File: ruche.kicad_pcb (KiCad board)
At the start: 2 copper layers, 61 x 100 mm, 68 parts, among them IC1 CN3791, IC2 MAX17048G+, IC3 L86-M33, IC4 SHT41-AD1B-R3, J1 Conn_01x02, J10 Conn_01x04, J11 Conn_01x04, J12 Conn_01x04, J13 Micro_SD_Card, J2 Conn_01x04, J3 Conn_01x03, J4 Conn_01x04, J5 Conn_01x04, J6 Conn_01x02, J7 Conn_01x02, J8 Conn_01x03, J9 Conn_01x03, Q1 AO3401A, U1 MKRWAN_1310, U2 MS5611-01BA, U3 XC6220B331MR

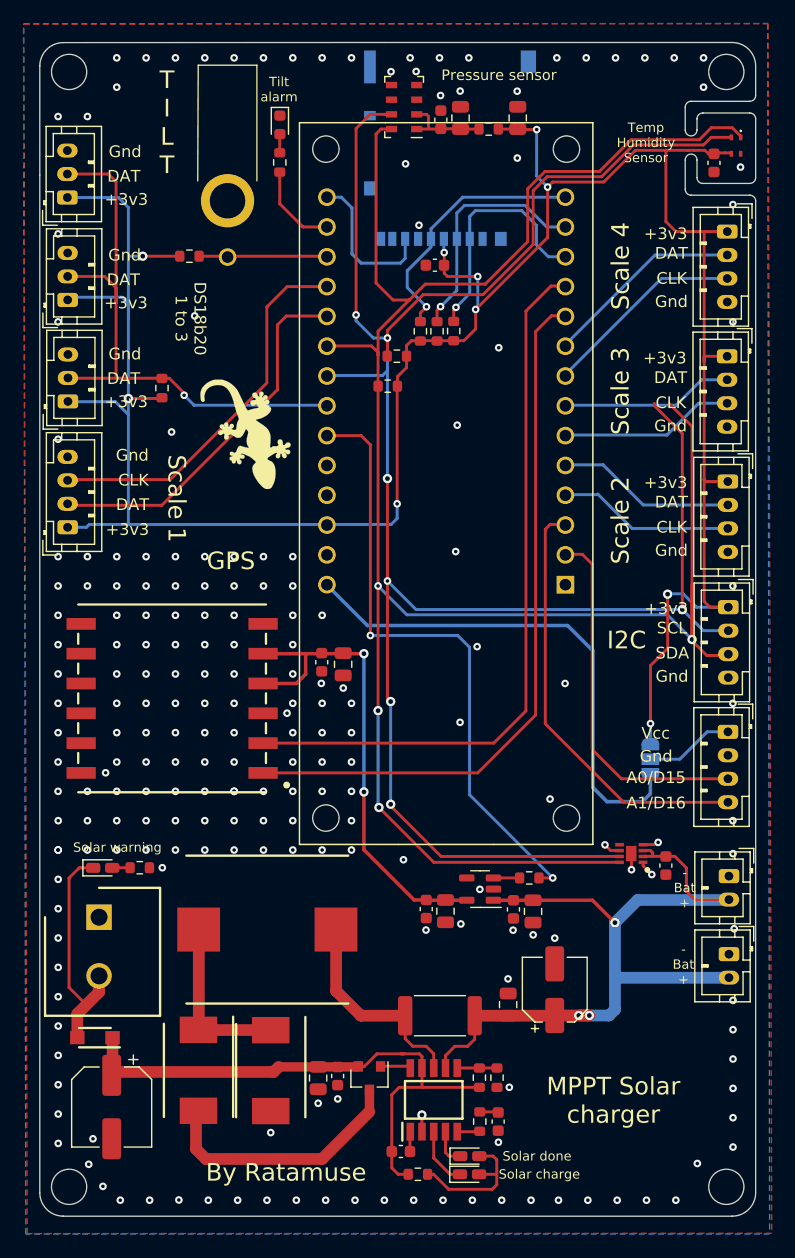
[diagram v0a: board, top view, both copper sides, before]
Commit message: Changement des pins
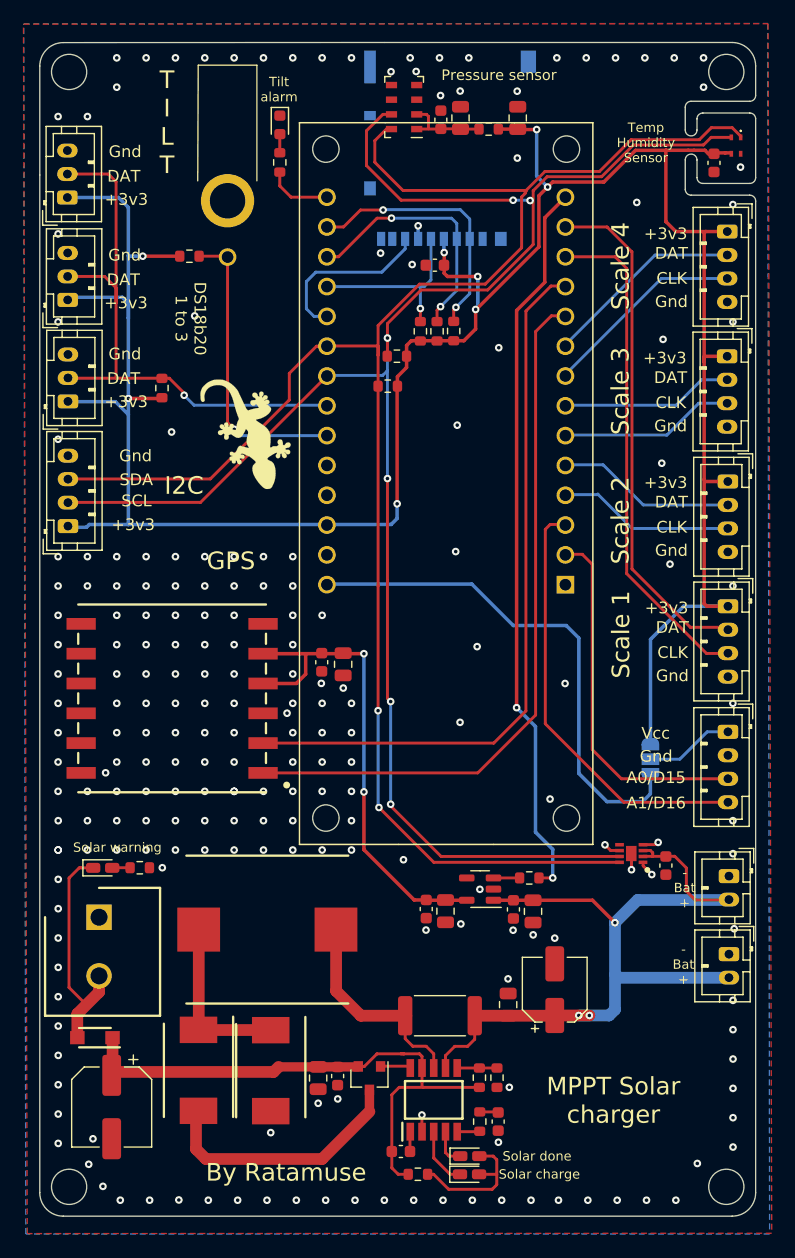
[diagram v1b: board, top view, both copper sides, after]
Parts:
- moved J5 56.7 mm to (98.9, 110.3), turned to 90 degrees
- moved J2 56.7 mm to (155.1, 117.1), turned to -90 degrees
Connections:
- U1 pad 12: SD3-CS-D6 -> CLK1
- U1 pad 13: CMD-MOSI-D3 -> DAT1
- U1 pad 14: CLK-SCK-D4 -> Start_GPS
- U1 pad 15: SDO-MISO-D5 -> Tilt_led_alarm
- U1 pad 16: Tilt_led_alarm -> SD3-CS-D6
- U1 pad 17: INT1 -> CMD-MOSI-D3
- U1 pad 18: CLK1 -> CLK-SCK-D4
- U1 pad 19: DAT1 -> SDO-MISO-D5
- U1 pad 23: Start_GPS -> INT1
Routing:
- net SDA: track 185.1 -> 155.3 mm, vias 4 -> 2
- net SCL: track 180.8 -> 155.3 mm, vias 7 -> 6
- net INT1: track 11.0 -> 25.7 mm, vias 0 -> 1
- net DAT1: track 32.2 -> 43.9 mm
- net CLK1: track 33.1 -> 43.1 mm
- net Start_GPS: track 52.9 -> 62.2 mm
- net CLK-SCK-D4: track 22.5 -> 15.5 mm
- net +3V3: track 219.9 -> 217.6 mm, vias 10 -> 8
- net Tilt_led_alarm: track 7.54 -> 5.59 mm
- net SD3-CS-D6: track 20.5 -> 22.4 mm, vias 1 -> 2
- net SDO-MISO-D5: track 13.1 -> 14.8 mm
- net CMD-MOSI-D3: track 20.2 -> 21.7 mm, vias 1 -> 2
- net GND: track 7.00 -> 8.10 mm, vias 214 -> 219

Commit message: Modification routage
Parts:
- moved C18 1.73 mm to (129.3, 143.1)
- moved C17 1.72 mm to (131.2, 143.0)
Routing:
- net GND: track 8.10 -> 9.33 mm, vias 219 -> 218

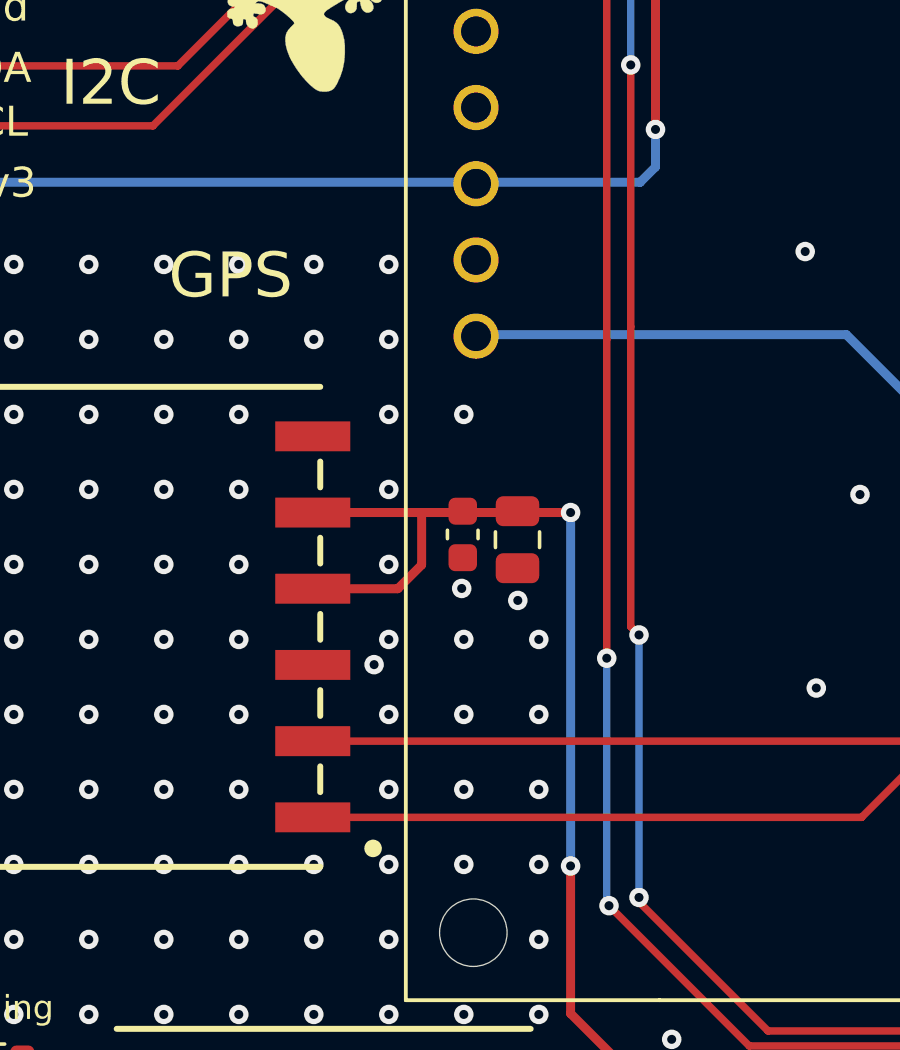
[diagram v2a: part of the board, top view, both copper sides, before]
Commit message: Add GPS backup power supply
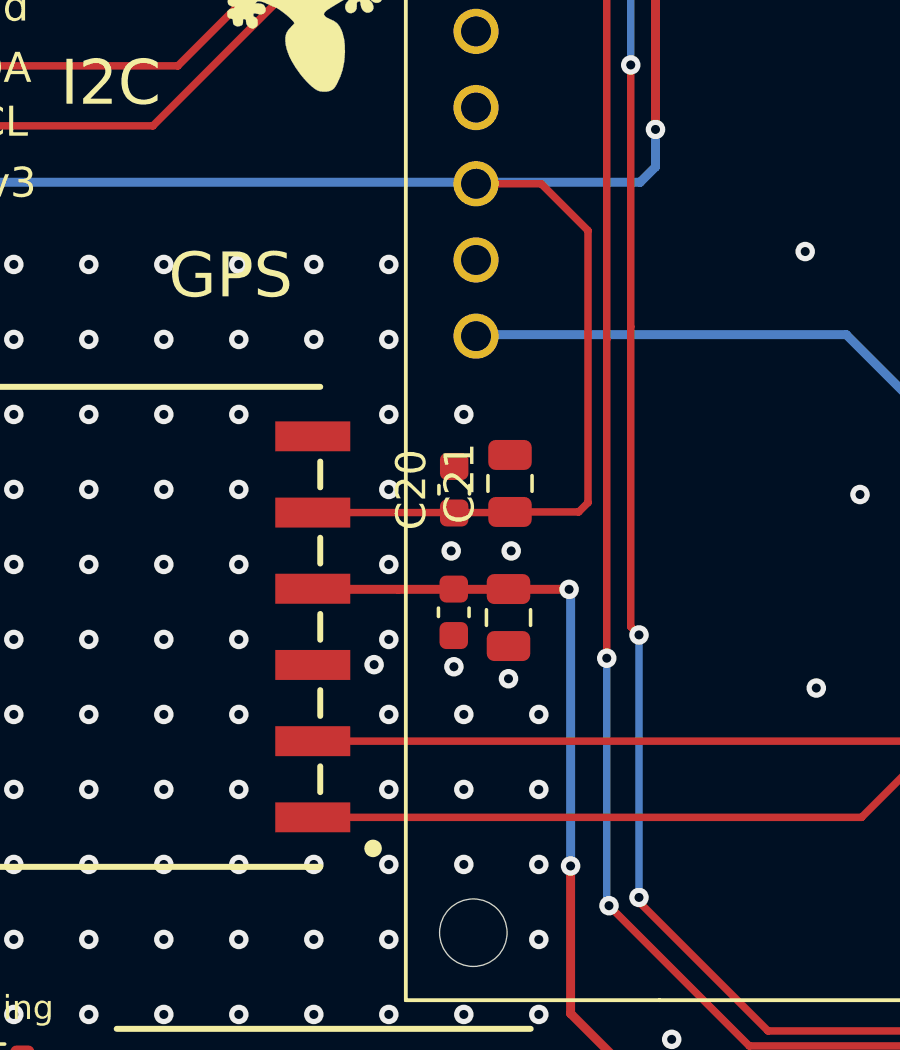
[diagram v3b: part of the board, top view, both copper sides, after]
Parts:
- added C20: 0.1µF, Capacitor_SMD:C_0603_1608Metric, F.Cu at (120.2, 120.4)
- added C21: 10µF, Capacitor_SMD:C_0805_2012Metric, F.Cu at (122.1, 120.2)
- moved C11 2.61 mm to (122.0, 124.7)
- moved C6 2.61 mm to (120.2, 124.5)
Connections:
- net CLK-SCK-D4 renamed CLK-SCK-D9
- net CMD-MOSI-D3 renamed CMD-MOSI-D8
- net SD3-CS-D6 renamed SD3-CS-D7
- net SDO-MISO-D5 renamed SDO-MISO-D10
- IC3 pad 5: VCC_GPS -> +3V3
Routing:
- net +3V3: track 217.6 -> 240.3 mm
- net VCC_GPS: track 45.2 -> 33.2 mm

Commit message: Add graphics
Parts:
- added G***: LOGO, Empreintes:bee, F.Cu at (150.0, 158.7)
- added G***: LOGO, Empreintes:bee large, B.Cu at (110.4, 100.3)
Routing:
- net GND: vias 218 -> 215

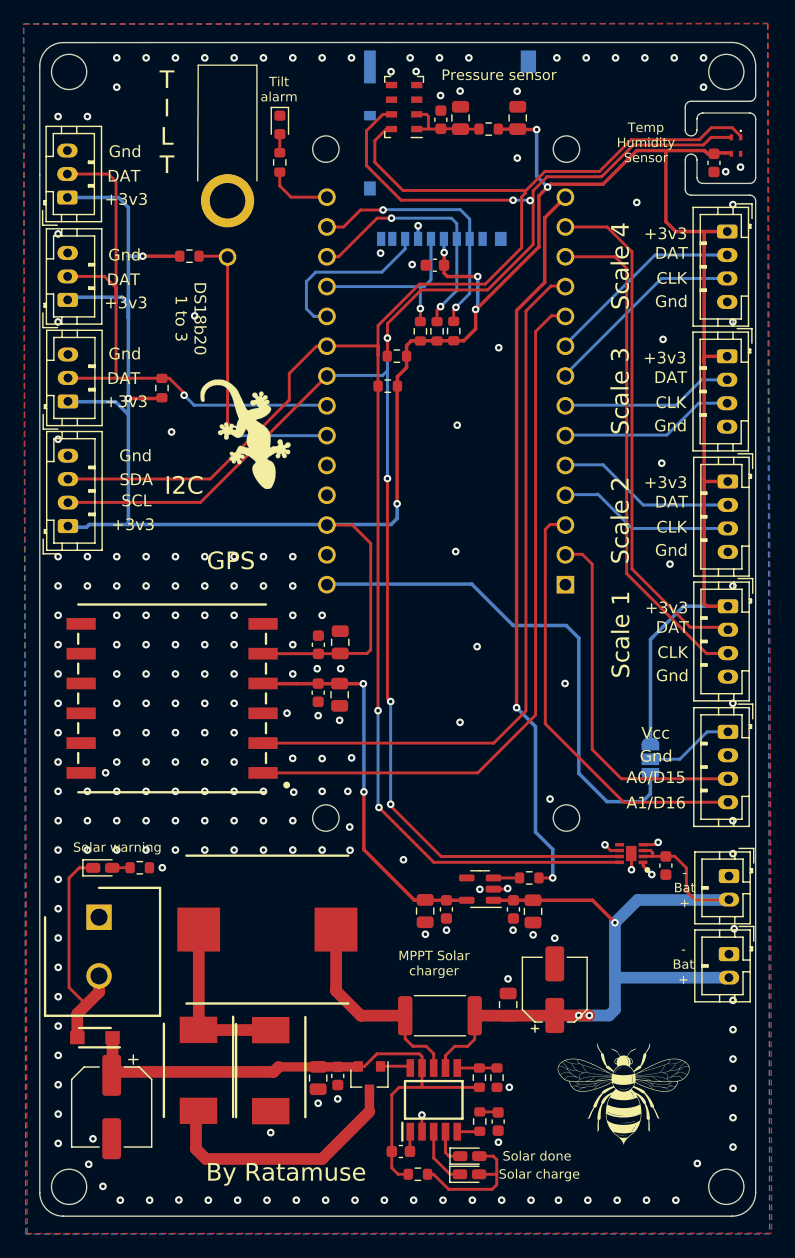
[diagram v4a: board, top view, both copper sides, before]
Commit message: add temp sensor
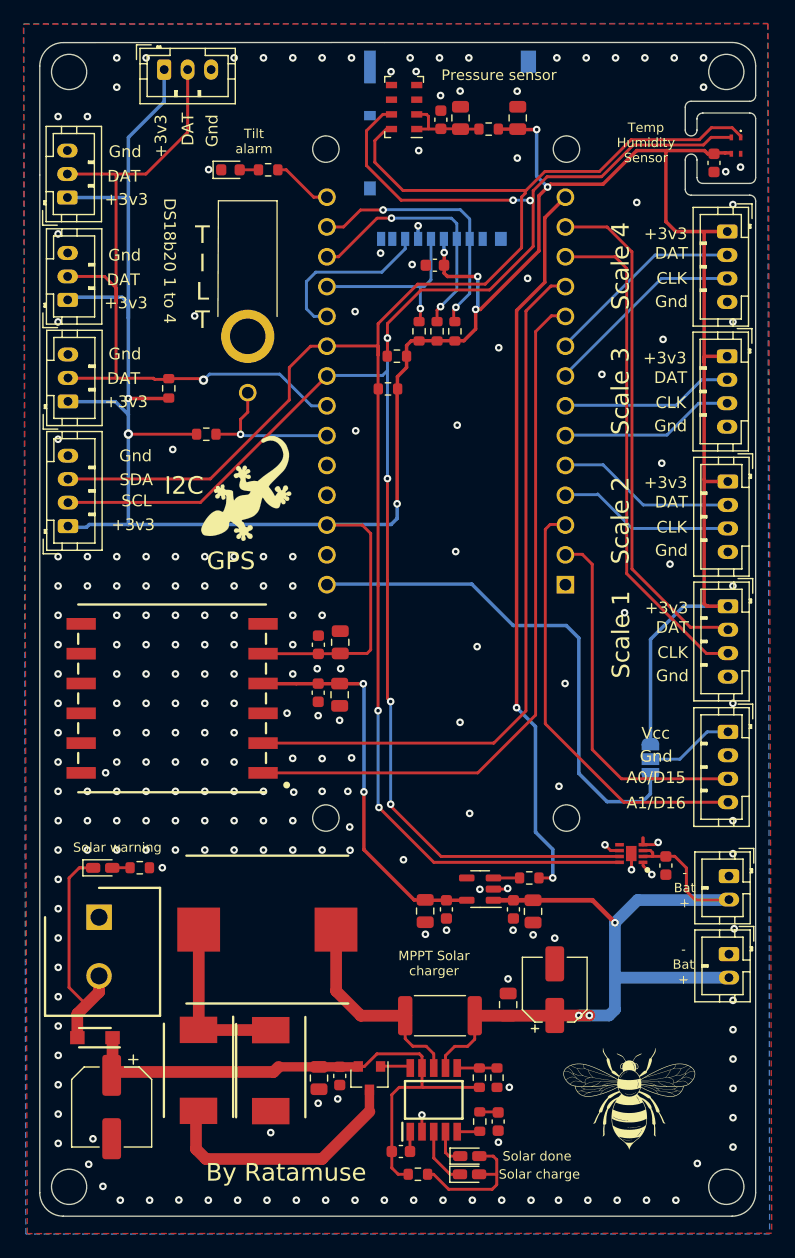
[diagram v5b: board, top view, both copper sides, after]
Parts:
- added J14: Conn_01x03, Connector_JST:JST_PH_B3B-PH-K_1x03_P2.00mm_Vertical, F.Cu at (107.1, 71.4)
- moved G*** 17.7 mm to (104.8, 83.5), turned to 180 degrees
- moved R10 15.2 mm to (110.7, 102.5)
- moved S1 11.7 mm to (114.2, 95.0)
- moved D7 5.69 mm to (112.8, 80.0), turned to 0 degrees
- moved G*** 4.97 mm to (114.0, 107.5), turned to -160 degrees
- moved R11 1.17 mm to (116.0, 80.0), turned to 0 degrees
- moved G*** 0.64 mm to (150.5, 159.1)
- moved R9 0.58 mm to (107.5, 98.6)
- moved R8 0.24 mm to (126.2, 98.6)
- moved C2 0.17 mm to (122.1, 157.2)
- moved R15 0.11 mm to (128.8, 93.7)
- moved R13 0.10 mm to (131.9, 93.7)
- moved C3 0.07 mm to (120.3, 157.3)
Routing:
- net +3V3: track 240.3 -> 255.7 mm
- net DS18b20: track 50.0 -> 63.7 mm
- net INT1: track 25.4 -> 13.3 mm
- net GND: track 9.33 -> 9.91 mm, vias 215 -> 221
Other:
- board text added: "DS18b20 1 to 4"
- board text added: "Spare GPIO"
- board text removed: "DS18b20 1 to 3"

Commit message: diverses modifications
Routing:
- net SCL: track 155.4 -> 156.8 mm
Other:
- board size 61 x 100 mm -> 61 x 99.9 mm
- board text added: "Ratamuse"
- board text removed: "By Ratamuse"

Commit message: V0.2
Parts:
- added FID1: Fiducial, Fiducial:Fiducial_1mm_Mask3mm, F.Cu at (116.2, 73.3)
- added FID2: Fiducial, Fiducial:Fiducial_1mm_Mask3mm, F.Cu at (147.9, 73.5)
- added FID3: Fiducial, Fiducial:Fiducial_1mm_Mask3mm, F.Cu at (150.0, 165.0)
- added FID4: Fiducial, Fiducial:Fiducial_1mm_Mask3mm, F.Cu at (107.2, 165.2)
- added G***: LOGO, Empreintes:alvéoles, B.Cu at (110.3, 106.4)
- moved R10 2.77 mm to (109.1, 100.2), turned to -90 degrees
- moved G*** 1.70 mm to (130.3, 142.7)
- moved G*** 0.90 mm to (104.9, 82.6)
- moved R9 0.09 mm to (107.5, 98.5)
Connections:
- U1 pad 10: RX_GPS -> INT1
- U1 pad 11: TX_GPS -> DS18b20
- U1 pad 22: DS18b20 -> TX_GPS
- U1 pad 23: INT1 -> RX_GPS
- U2 pad 7: SCL -> SDA
- U2 pad 8: SDA -> SCL
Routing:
- net DS18b20: track 63.7 -> 86.4 mm
- net INT1: track 13.3 -> 35.7 mm, vias 1 -> 0
- net TX_GPS: track 61.9 -> 46.4 mm, vias 0 -> 1
- net RX_GPS: track 61.0 -> 48.0 mm, vias 0 -> 1
- net +3V3: track 255.7 -> 251.3 mm, vias 8 -> 7
- net SDA: track 155.9 -> 159.0 mm
- net SCL: track 156.8 -> 154.8 mm
- net GND: vias 221 -> 223
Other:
- board text added: "Open beehive scale board V0.2 by Ratamuse"
- board text removed: "Open beehive scale board V0.1 by Ratamuse"
